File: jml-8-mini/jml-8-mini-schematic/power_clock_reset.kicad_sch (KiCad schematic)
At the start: 20 parts, among them J1 BarrelJack, SW1 SW_Push, SW2 SW_Push_DPDT, U10 74LS74, U11 NE555P, U6 74LS04, X1 8MHz, X2 2.4576MHz

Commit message: add to info section of schematic
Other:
- company: (none) -> https://github.com/jac-oblong/jml
- title: (none) -> JML-8 Mini Schematic
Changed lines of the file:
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@@
   (paper "A4")
   (title_block
+    (title "JML-8 Mini Schematic")
     (date "2023-10-02")
     (rev "A")
-    (comment 1 "Author: Jacob Long")
+    (company "https://github.com/jac-oblong/jml")
+    (comment 1 "Design of Z80 based microcomputer")
+    (comment 3 "Released under MIT License")
+    (comment 4 "Created by: Jacob Long (https://github.com/jac-oblong)")
   )
   (junction (at 63.5 144.145) (diameter 0) (color 0 0 0 0)

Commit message: update info section of schematic
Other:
- company: https://github.com/jac-oblong/jml -> https://github.com/jac-oblong/JML
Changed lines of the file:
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@@
     (date "2023-10-02")
     (rev "A")
-    (company "https://github.com/jac-oblong/jml")
+    (company "https://github.com/jac-oblong/JML")
     (comment 1 "Design of Z80 based microcomputer")
     (comment 3 "Released under MIT License")

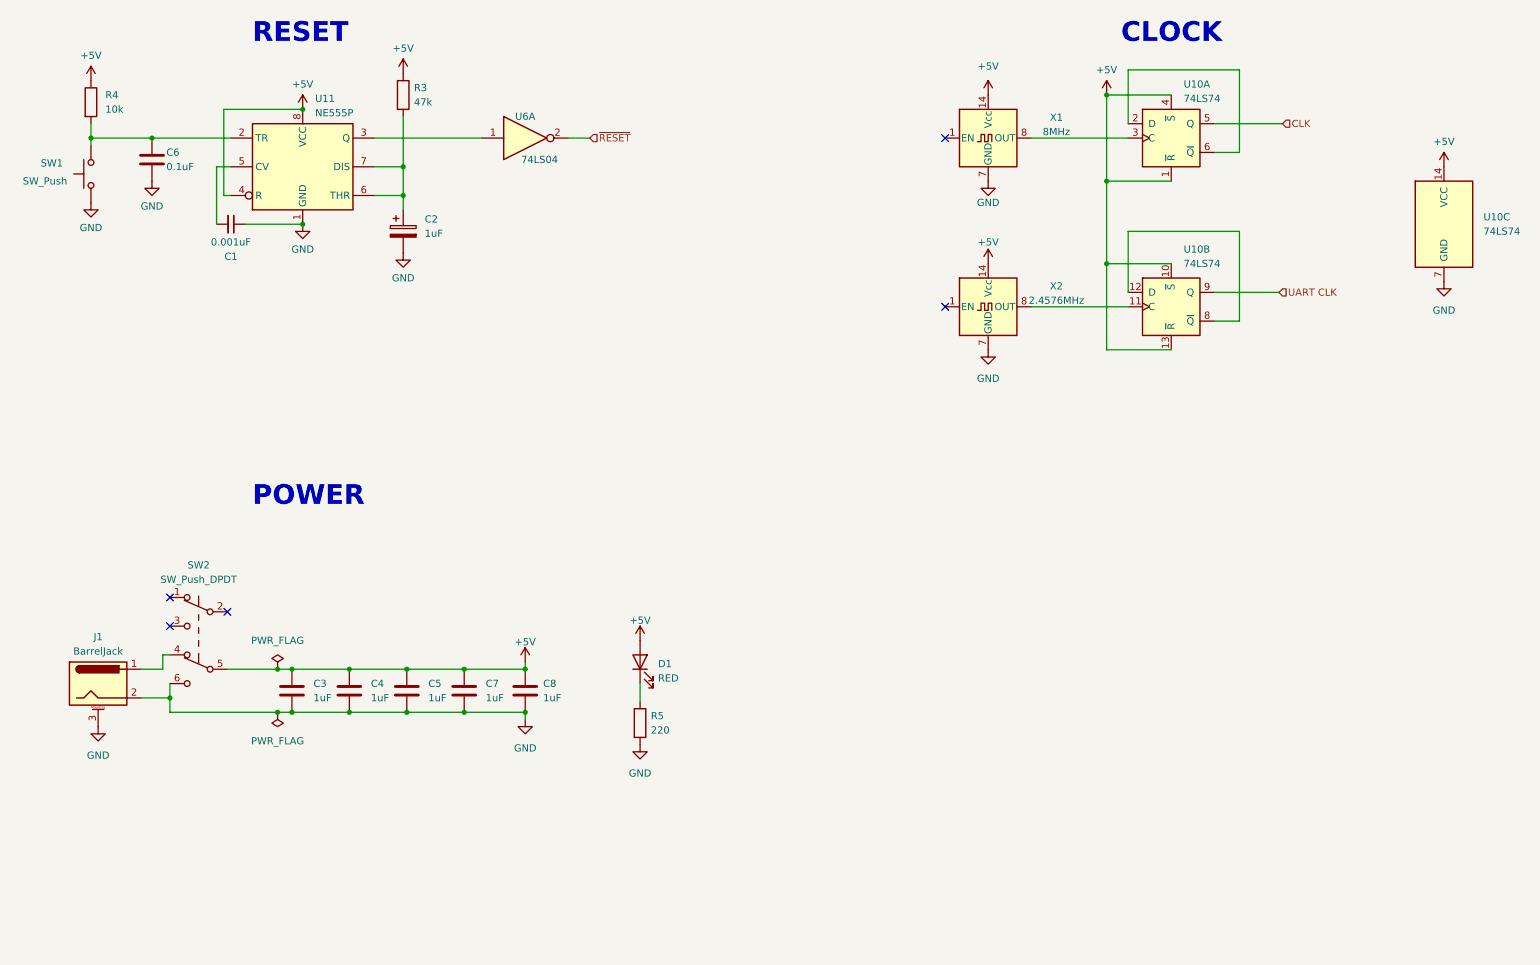
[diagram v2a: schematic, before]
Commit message: general "neatening" of schematics
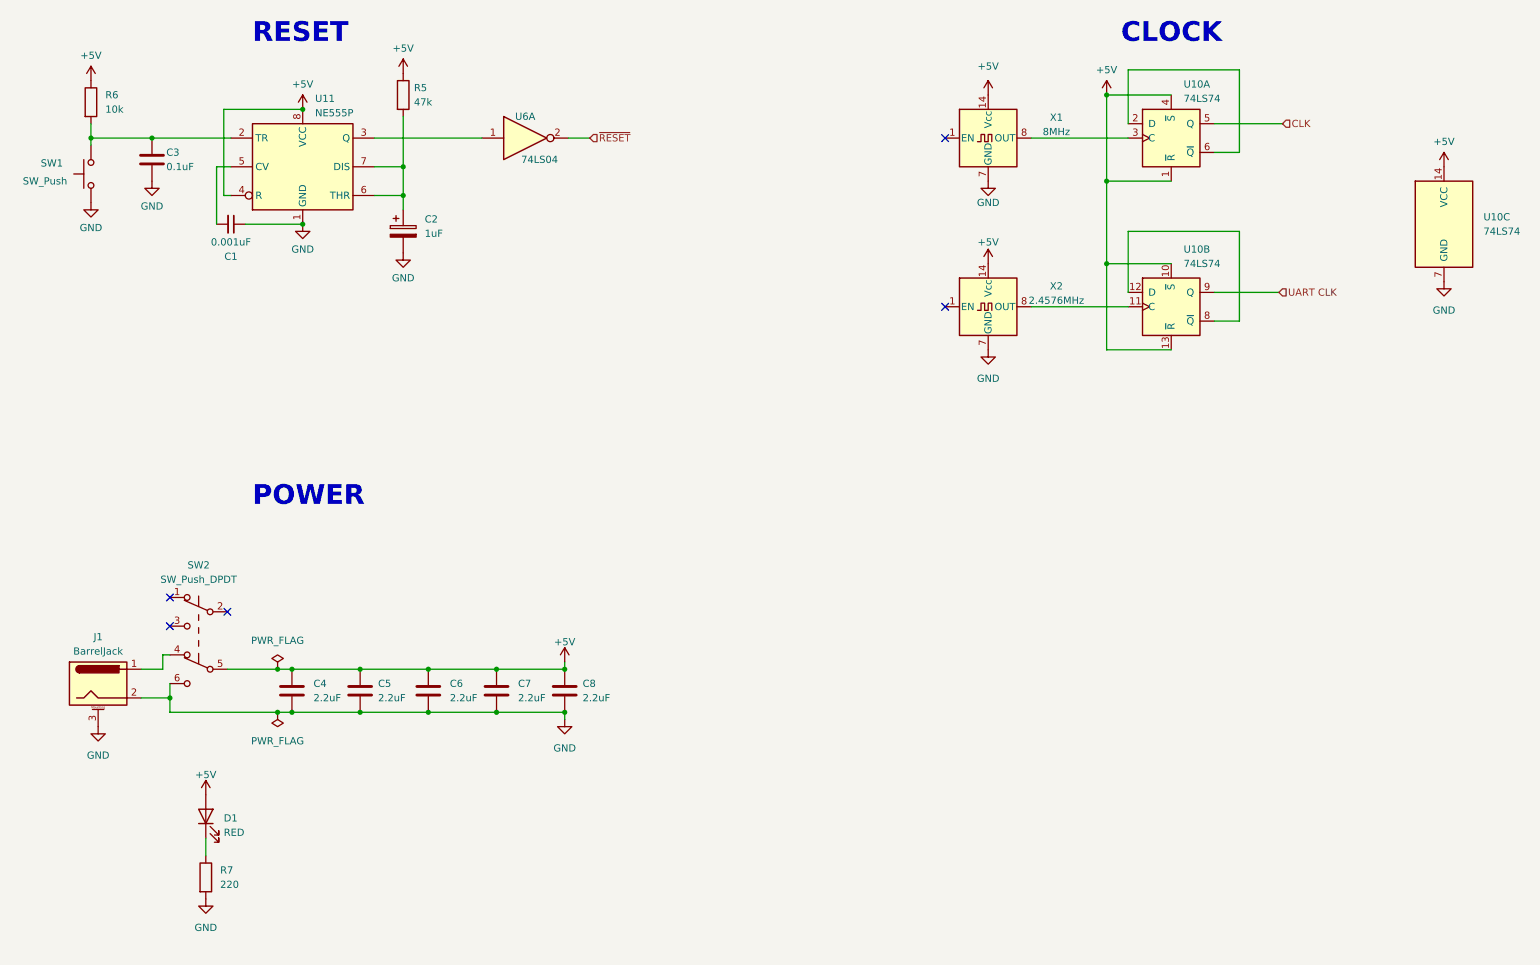
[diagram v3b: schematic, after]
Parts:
- C4: renamed from C3; value 1uF -> 2.2uF
- C5: renamed from C4; value 1uF -> 2.2uF
- C6: renamed from C5; value 1uF -> 2.2uF
- C7, C8: value 1uF -> 2.2uF
- renumbered C6 to C3, R3 to R5, R4 to R6, R5 to R7
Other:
- moved on the sheet: C5, C6, C7, C8, D1, R7

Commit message: change some footprints
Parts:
- R5, R6, R7: footprint Resistor_THT:R_Axial_DIN0207_L6.3mm_D2.5mm_P10.16mm_Horizontal -> Resistor_THT:R_Axial_DIN0207_L6.3mm_D2.5mm_P7.62mm_Horizontal
- U10, U6: footprint Package_DIP:DIP-14_W7.62mm_LongPads -> Package_DIP:DIP-14_W7.62mm_Socket_LongPads
- U11: footprint Package_DIP:DIP-8_W7.62mm -> Package_DIP:DIP-8_W7.62mm_Socket_LongPads
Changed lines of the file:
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@@
       (effects (font (size 1.27 1.27)) (justify left))
     )
-    (property "Footprint" "Package_DIP:DIP-14_W7.62mm_LongPads" (at 221.615 72.39 0)
+    (property "Footprint" "Package_DIP:DIP-14_W7.62mm_Socket_LongPads" (at 221.615 72.39 0)
       (effects (font (size 1.27 1.27)) hide)
     )
@@
       (effects (font (size 1.27 1.27)) (justify left))
     )
-    (property "Footprint" "Package_DIP:DIP-14_W7.62mm_LongPads" (at 269.875 57.785 0)
+    (property "Footprint" "Package_DIP:DIP-14_W7.62mm_Socket_LongPads" (at 269.875 57.785 0)
       (effects (font (size 1.27 1.27)) hide)
     )
@@
       (effects (font (size 1.27 1.27)) (justify left))
     )
-    (property "Footprint" "Resistor_THT:R_Axial_DIN0207_L6.3mm_D2.5mm_P10.16mm_Horizontal" (at 49.022 173.355 90)
+    (property "Footprint" "Resistor_THT:R_Axial_DIN0207_L6.3mm_D2.5mm_P7.62mm_Horizontal" (at 49.022 173.355 90)
       (effects (font (size 1.27 1.27)) hide)
     )
@@
       (effects (font (size 1.27 1.27)) (justify left))
     )
-    (property "Footprint" "Resistor_THT:R_Axial_DIN0207_L6.3mm_D2.5mm_P10.16mm_Horizontal" (at 83.947 34.925 90)
+    (property "Footprint" "Resistor_THT:R_Axial_DIN0207_L6.3mm_D2.5mm_P7.62mm_Horizontal" (at 83.947 34.925 90)
       (effects (font (size 1.27 1.27)) hide)
     )
@@
       (effects (font (size 1.27 1.27)) (justify left))
     )
-    (property "Footprint" "Package_DIP:DIP-14_W7.62mm_LongPads" (at 221.615 42.545 0)
+    (property "Footprint" "Package_DIP:DIP-14_W7.62mm_Socket_LongPads" (at 221.615 42.545 0)
       (effects (font (size 1.27 1.27)) hide)
     )
@@
       (effects (font (size 1.27 1.27)) (justify left))
     )
-    (property "Footprint" "Resistor_THT:R_Axial_DIN0207_L6.3mm_D2.5mm_P10.16mm_Horizontal" (at 28.702 36.195 90)
+    (property "Footprint" "Resistor_THT:R_Axial_DIN0207_L6.3mm_D2.5mm_P7.62mm_Horizontal" (at 28.702 36.195 90)
       (effects (font (size 1.27 1.27)) hide)
     )
@@
       (effects (font (size 1.27 1.27)))
     )
-    (property "Footprint" "Package_DIP:DIP-14_W7.62mm_LongPads" (at 107.315 42.545 0)
+    (property "Footprint" "Package_DIP:DIP-14_W7.62mm_Socket_LongPads" (at 107.315 42.545 0)
       (effects (font (size 1.27 1.27)) hide)
     )
@@
       (effects (font (size 1.27 1.27)) (justify left))
     )
-    (property "Footprint" "Package_DIP:DIP-8_W7.62mm" (at 84.455 57.785 0)
-      (effects (font (size 1.27 1.27)) hide)
-    )
+    (property "Footprint" "Package_DIP:DIP-8_W7.62mm_Socket_LongPads" (at 84.455 57.785 0)
+      (effects (font (size 1.27 1.27)) hide)
+    )

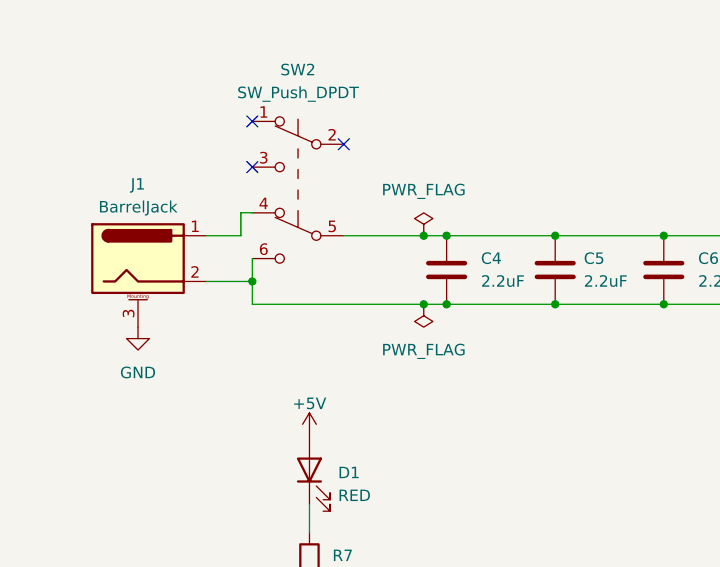
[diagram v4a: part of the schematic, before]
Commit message: add resistor so caps discharge slower when power cuts off
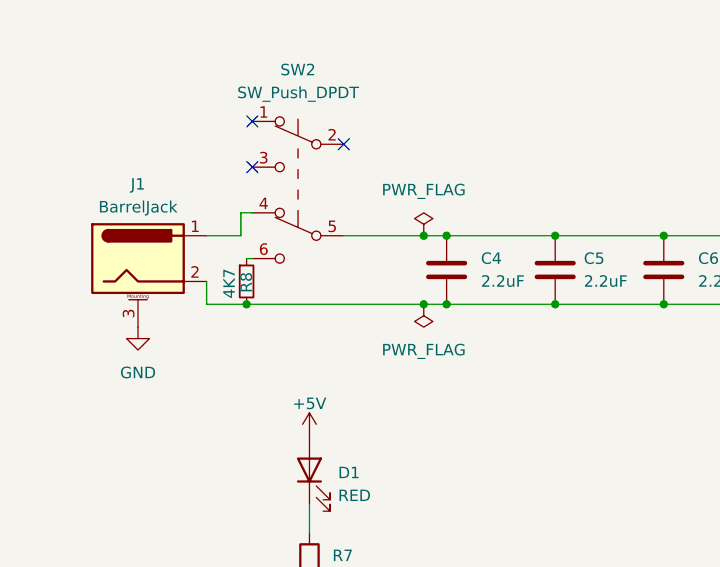
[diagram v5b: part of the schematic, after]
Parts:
- added R8: 4K7, Resistor_THT:R_Axial_DIN0207_L6.3mm_D2.5mm_P7.62mm_Horizontal, symbol Device:R_Small
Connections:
- net GND: now also R8.2; no longer SW2.6 (C)
- new net: R8.1, SW2.6 (C)
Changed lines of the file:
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@@
   (junction (at 85.725 47.625) (diameter 0) (color 0 0 0 0)
   )
-  (junction (at 44.45 141.605) (diameter 0) (color 0 0 0 0)
-  )
   (junction (at 210.185 64.77) (diameter 0) (color 0 0 0 0)
   )
@@
   )
   (junction (at 30.48 42.545) (diameter 0) (color 0 0 0 0)
+  )
+  (junction (at 43.815 144.145) (diameter 0) (color 0 0 0 0)
   )
   (junction (at 210.185 50.165) (diameter 0) (color 0 0 0 0)
@@
     (stroke (width 0) (type default))
   )
-  (wire (pts (xy 39.37 141.605) (xy 44.45 141.605))
-    (stroke (width 0) (type default))
-  )
   (wire (pts (xy 213.995 69.85) (xy 213.995 59.055))
     (stroke (width 0) (type default))
@@
     (stroke (width 0) (type default))
   )
-  (wire (pts (xy 44.45 144.145) (xy 44.45 141.605))
+  (wire (pts (xy 39.37 144.145) (xy 39.37 141.605))
     (stroke (width 0) (type default))
   )
@@
     (stroke (width 0) (type default))
   )
+  (wire (pts (xy 43.815 139.065) (xy 44.45 139.065))
+    (stroke (width 0) (type default))
+  )
   (wire (pts (xy 229.235 69.85) (xy 240.665 69.85))
     (stroke (width 0) (type default))
@@
     (stroke (width 0) (type default))
   )
-  (wire (pts (xy 44.45 144.145) (xy 63.5 144.145))
+  (wire (pts (xy 39.37 144.145) (xy 43.815 144.145))
     (stroke (width 0) (type default))
   )
@@
     (stroke (width 0) (type default))
   )
-  (wire (pts (xy 44.45 139.065) (xy 44.45 141.605))
-    (stroke (width 0) (type default))
-  )
   (wire (pts (xy 210.185 64.77) (xy 210.185 80.01))
     (stroke (width 0) (type default))
   )
   (wire (pts (xy 66.04 144.145) (xy 78.105 144.145))
+    (stroke (width 0) (type default))
+  )
+  (wire (pts (xy 43.815 144.145) (xy 63.5 144.145))
     (stroke (width 0) (type default))
   )
@@
         )
       )
+    )
+  )
+  (symbol (lib_id "Device:R_Small") (at 43.815 141.605 0) (unit 1)
+    (in_bom yes) (on_board yes) (dnp no)
+    (property "Reference" "R8" (at 43.815 142.875 90)
+      (effects (font (size 1.27 1.27)) (justify left))
+    )
+    (property "Value" "4K7" (at 41.91 143.51 90)
+      (effects (font (size 1.27 1.27)) (justify left))
+    )
+    (property "Footprint" "Resistor_THT:R_Axial_DIN0207_L6.3mm_D2.5mm_P7.62mm_Horizontal" (at 43.815 141.605 0)
+      (effects (font (size 1.27 1.27)) hide)
+    )
+    (property "Datasheet" "~" (at 43.815 141.605 0)
+      (effects (font (size 1.27 1.27)) hide)
+    )
+    (pin "1")
+    (pin "2")
+    (instances
+      (project "jml-8-mini"
+        (path "/7f93abb4-2372-4a9e-a664-5edb67349db4/024bfdd5-d810-4269-aa23-d376373ff9a1"
+          (reference "R8") (unit 1)
+        )
+      )

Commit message: lots of updates to schematic to make pcb routing easier, start on pcb design
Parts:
- R5: value 47k -> 47K
- R6: value 10k -> 10K
- R7: value 220 -> 2K2
- SW1: value SW_Push -> Reset
- SW2: value SW_Push_DPDT -> Power
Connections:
- net +5V: now also SW2.2 (B); no longer SW2.5 (B)
- net 2.4576MHz: now reaches U10.11 (C), X2.8 (OUT)
- net DFFB_DataIn: now reaches U10.12 (D), U10.8 (~{Q})
- net 555Trigger: now reaches C3.1, R6.2, SW1.2, U11.2 (TR)
- net LED_TO_R: now reaches D1.1 (K), R7.1
- net at SW2.6 (C): no longer R8.1
- net at SW2.4 (A): no longer J1.1
- net 555Dis/Thr: now reaches C2.1, R5.2, U11.6 (THR), U11.7 (DIS)
- net DFFA_DataIn: now reaches U10.2 (D), U10.6 (~{Q})
- net 8MHz: now reaches U10.3 (C), X1.8 (OUT)
- net SW_TO_R: now reaches SW2.1 (A)
- net SW_TO_R: now also R8.1
- net PWR_IN: now reaches SW2.3 (C)
- net PWR_IN: now also J1.1
- net 555Out: now reaches U11.3 (Q), U6.1
- net 555Control: now reaches C1.2, U11.5 (CV)
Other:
- note added: "Decoupling Capacitor for each "main" IC (CPU, RAM, ROM, CTC, SIO)"
- note added: "Divide Crystal Oscillator freq by 2"
- note added: "Generate RESET Sig on Power-Up, lasts ~50ms"
- moved on the sheet: C1, C2, C3, R5, R6, R8, SW1, SW2, U11, U6A
